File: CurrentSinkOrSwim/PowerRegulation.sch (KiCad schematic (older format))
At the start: 6 parts, among them U401 LM2931ACDG

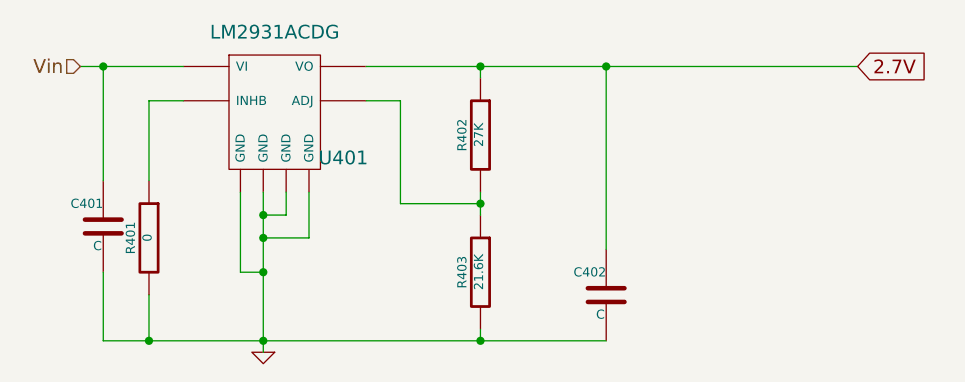
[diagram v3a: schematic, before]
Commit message: Actualizando información de los componentes y creando el BOM
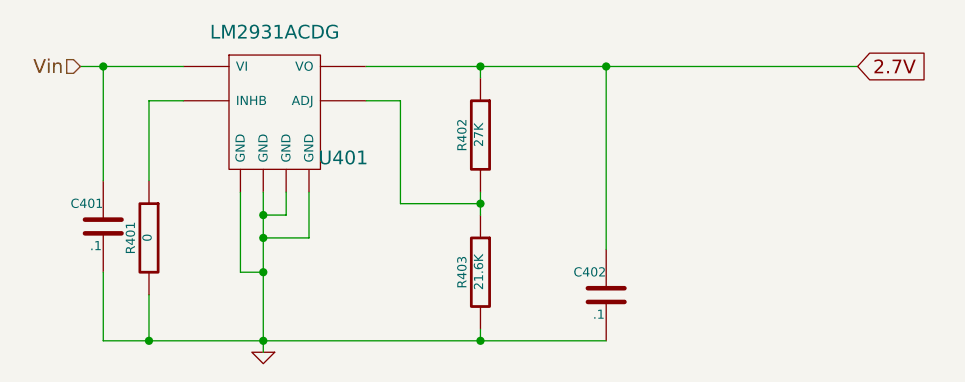
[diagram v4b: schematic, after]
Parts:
- C401, C402: value C -> .1
- U401: MFG Name (none) -> LM2931ACDG
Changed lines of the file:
@@
 Sheet 4 4
 Title ""
-Date "24 sep 2015"
+Date "1 oct 2015"
 Rev ""
 Comp ""
@@
 P 5950 4000
 F 0 "C402" H 5950 4100 40  0000 L CNN
-F 1 "C" H 5956 3915 40  0000 L CNN
+F 1 ".1" H 5956 3915 40  0000 L CNN
 F 2 "~" H 5988 3850 30  0000 C CNN
 F 3 "~" H 5950 4000 60  0000 C CNN
@@
 P 3750 3700
 F 0 "C401" H 3750 3800 40  0000 L CNN
-F 1 "C" H 3756 3615 40  0000 L CNN
+F 1 ".1" H 3756 3615 40  0000 L CNN
 F 2 "~" H 3788 3550 30  0000 C CNN
 F 3 "~" H 3750 3700 60  0000 C CNN
@@
 F 2 "~" H 4450 3000 60  0000 C CNN
 F 3 "~" H 4450 3000 60  0000 C CNN
+F 4 "LM2931ACDG" H 4500 3150 60  0001 C CNN "MFG Name"
 	1    4500 3150
 	1    0    0    -1
